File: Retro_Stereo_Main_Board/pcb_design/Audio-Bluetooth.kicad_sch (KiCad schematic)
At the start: 1 part, among them U8 Microchip_BM83

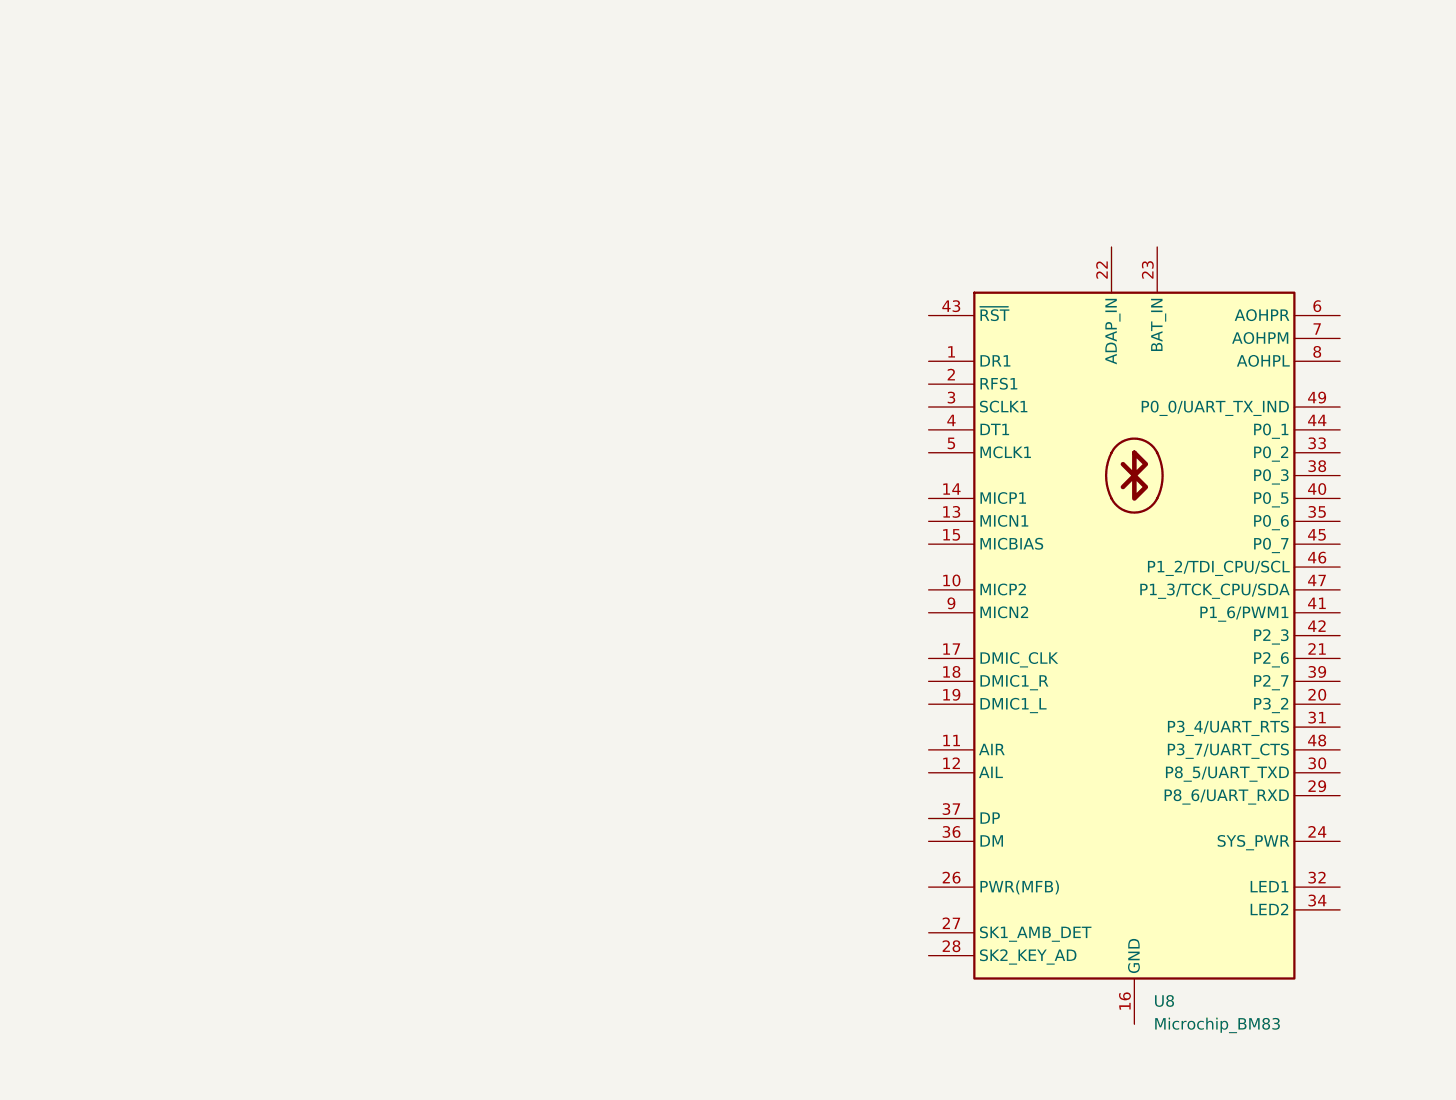
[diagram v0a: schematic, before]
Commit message: Complete TEF6686 schematic page
- Start Bluetooth input design

Signed-off-by: Francisco <fran.testa07Qgmail.com>
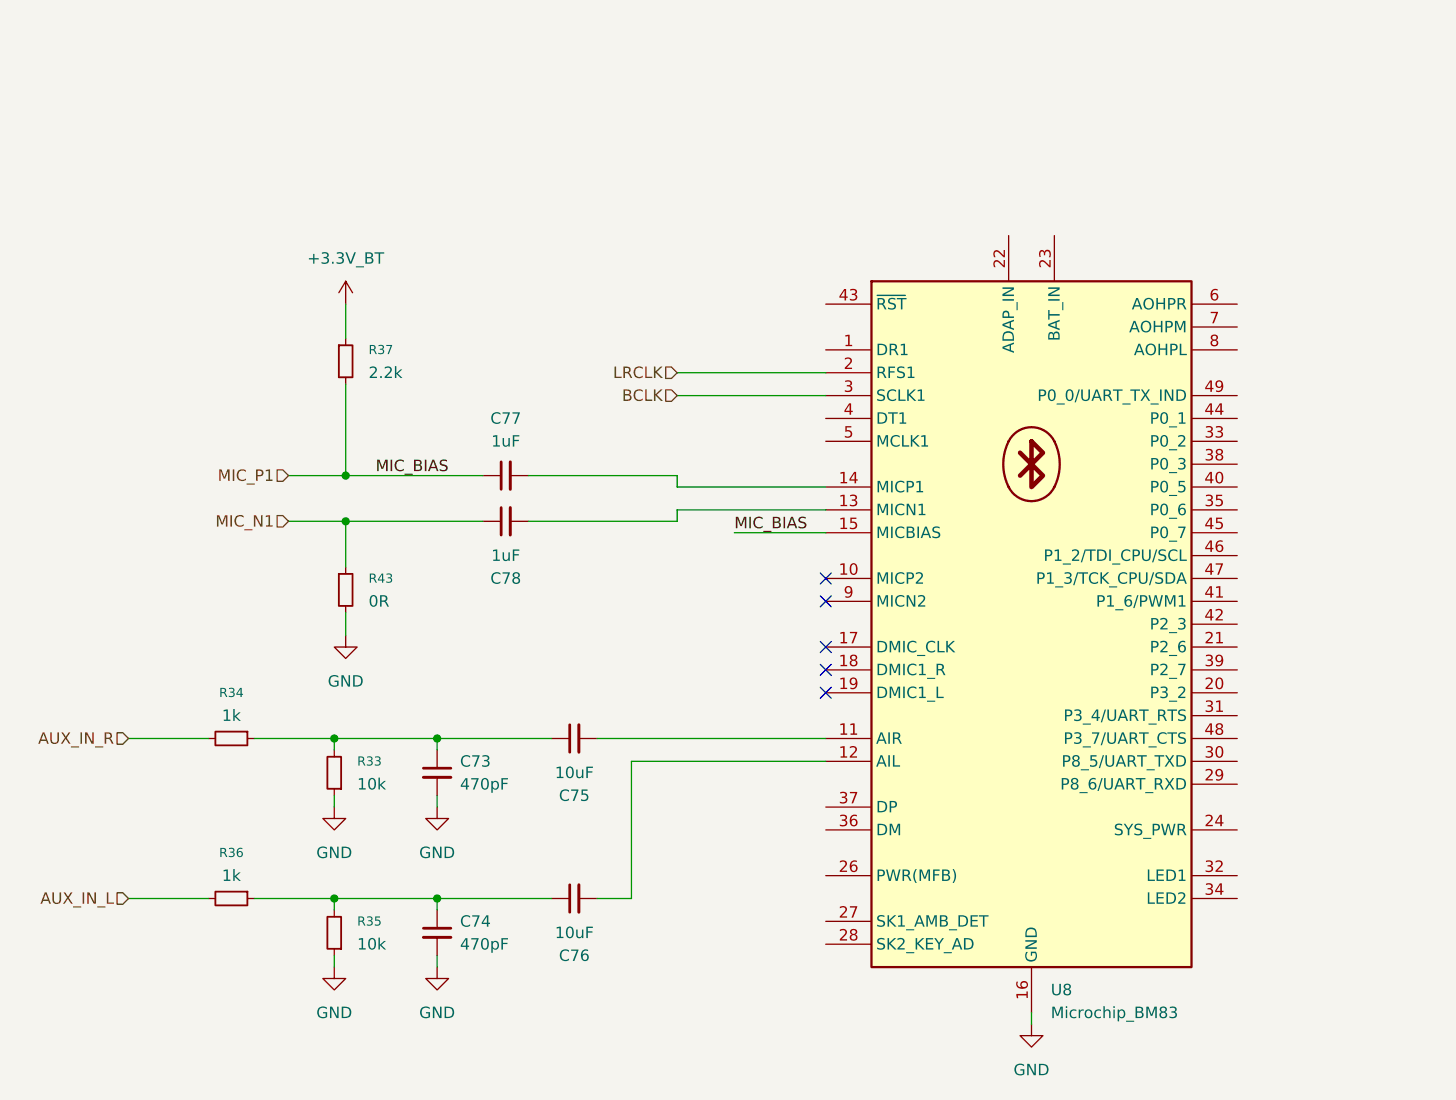
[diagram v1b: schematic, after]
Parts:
- added C73, C74: 470pF, symbol Device:C_Small
- added C75, C76: 10uF, symbol Device:C_Small
- added C77, C78: 1uF, symbol Device:C_Small
- added R33, R35: 10k, symbol Device:R_Small
- added R34, R36: 1k, symbol Device:R_Small
- added R37: 2.2k, symbol Device:R_Small
- added R43: 0R, symbol Device:R_Small
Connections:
- net at U8.11 (AIR): now also C75.2
- net at U8.12 (AIL): now also C76.2
- net at U8.13 (MICN1): now also C78.2
- net at U8.14 (MICP1): now also C77.2
- net MIC_P1: now reaches U8.15 (MICBIAS)
- net MIC_P1: now also C77.1, R37.2
- net GND: now reaches U8.16 (GND), U8.50 (GND), U8.56 (GND), U8.57 (GND)
- net GND: now also C73.2, C74.2, R33.1, R35.1, R43.2
- net LRCLK: now reaches U8.2 (RFS1)
- net BCLK: now reaches U8.3 (SCLK1)
- new net: C74.1, C76.1, R35.2, R36.1
- new net: C73.1, C75.1, R33.2, R34.1
- new net +3.3V_BT: R37.1
- new net AUX_IN_L: R36.2
- new net AUX_IN_R: R34.2
- new net MIC_N1: C78.1, R43.1
- no-connect marks 0 -> 5
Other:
- moved on the sheet: U8

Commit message: Complete BT module sheet
Signed-off-by: Francisco <fran.testa07Qgmail.com>
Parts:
- added C79, C99: 100nF, Capacitor_SMD:C_0805_2012Metric, symbol Device:C_Small
- added C80: 1uF, Capacitor_SMD:C_0805_2012Metric, symbol Device:C_Small
- R43: value 0R -> 10k
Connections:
- net GND: now also C79.2, C80.2, C99.2; no longer R43.2
- net MIC_N1: no longer R43.1
- net MIC_P1: no longer U8.15 (MICBIAS)
- net AUX_JACK_DET: now reaches U8.20 (P3_2)
- net P2_6: now reaches U8.21 (P2_6)
- net +3.8V_BT: now reaches U8.23 (BAT_IN)
- net +3.8V_BT: now also R43.2, C79.1, C80.1
- net at U8.24 (SYS_PWR): now also C99.1
- net MFB: now reaches U8.26 (PWR(MFB))
- net UART_RXD: now reaches U8.29 (P8_6/UART_RXD)
- net UART_TXD: now reaches U8.30 (P8_5/UART_TXD)
- net UART_RTS: now reaches U8.31 (P3_4/UART_RTS)
- net P0_2: now reaches U8.33 (P0_2)
- net USB_D-: now reaches U8.36 (DM)
- net USB_D+: now reaches U8.37 (DP)
- net P0_3: now reaches U8.38 (P0_3)
- net P2_7: now reaches U8.39 (P2_7)
- net I2S_SD: now reaches U8.4 (DT1)
- net P0_5: now reaches U8.40 (P0_5)
- net P1_6: now reaches U8.41 (P1_6/PWM1)
- net P2_3: now reaches U8.42 (P2_3)
- net RST_IN: now reaches U8.43 (~{RST})
- net RST_IN: now also R43.1
- net P0_1: now reaches U8.44 (P0_1)
- net I2C_SCL: now reaches U8.46 (P1_2/TDI_CPU/SCL)
- net I2C_SDA: now reaches U8.47 (P1_3/TCK_CPU/SDA)
- net UART_CTS: now reaches U8.48 (P3_7/UART_CTS)
- net UART_TX_IND: now reaches U8.49 (P0_0/UART_TX_IND)
- net I2S_MCLK: now reaches U8.5 (MCLK1)
- net +3.3V_BT renamed MIC_BIAS
- net MIC_BIAS: now also U8.15 (MICBIAS)
- net BCLK renamed I2S_BCLK
- net LRCLK renamed I2S_LRCLK
- no-connect marks 5 -> 16
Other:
- moved on the sheet: R37
